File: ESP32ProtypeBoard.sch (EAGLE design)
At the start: 101 parts, among them IC1 SOIC-8, IC2 SI4431BDY, IC4 LMC555*, J10 POWER_JACKPTH_LOCK, Q1 MMBT3904*, Q2 MMBT3904, Q3 MMBT3904, U2 ESP-WROOM-32

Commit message: All connected
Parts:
- added J54: (no value), SparkFun-Connectors:CONN_10NO_SILK_PTH_FEMALE
- C2: device rcl:C-EUC1206K -> rcl:C-EUC1210
- J8: device SparkFun-Connectors:CONN_041X04_NO_SILK -> SparkFun-Connectors:CONN_111X11_NO_SILK
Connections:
- net +3V3: now also J17.4, J17.5
- net GND: now also J17.2
- net IO22: now also J17.7
- net IO23: now also J17.3
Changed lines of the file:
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@@
 <part name="R8" library="eagle-ltspice" library_urn="urn:adsk.eagle:library:217" deviceset="R" device="R1206" package3d_urn="urn:adsk.eagle:package:13301/1" value="470R"/>
 <part name="GND1" library="supply1" library_urn="urn:adsk.eagle:library:371" deviceset="GND" device=""/>
-<part name="C2" library="rcl" library_urn="urn:adsk.eagle:library:334" deviceset="C-EU" device="C1206K" package3d_urn="urn:adsk.eagle:package:23682/2" value="100uF"/>
+<part name="C2" library="rcl" library_urn="urn:adsk.eagle:library:334" deviceset="C-EU" device="C1210" package3d_urn="urn:adsk.eagle:package:23619/2" value="100uF"/>
 <part name="AMS1117-3.3" library="SparkFun-IC-Power" deviceset="V_REG_LD1117VXX" device="LD1117-SMD" value="3V3"/>
 <part name="GND11" library="supply1" library_urn="urn:adsk.eagle:library:371" deviceset="GND" device=""/>
@@
 <part name="J6" library="SparkFun-Connectors" deviceset="CONN_16" device="1X16_NO_SILK"/>
 <part name="J7" library="SparkFun-Connectors" deviceset="CONN_06X2" device="NO_SILK"/>
-<part name="J8" library="SparkFun-Connectors" deviceset="CONN_04" device="1X04_NO_SILK"/>
+<part name="J8" library="SparkFun-Connectors" library_urn="urn:adsk.eagle:library:513" deviceset="CONN_11" device="1X11_NO_SILK" package3d_urn="urn:adsk.eagle:package:38260/1"/>
 <part name="J9" library="SparkFun-Connectors" deviceset="CONN_04" device="1X04_NO_SILK"/>
 <part name="J17" library="SparkFun-Connectors" deviceset="CONN_07" device="NO_SILK"/>
@@
 <part name="GND26" library="supply1" library_urn="urn:adsk.eagle:library:371" deviceset="GND" device=""/>
 <part name="TP1" library="testpad" library_urn="urn:adsk.eagle:library:385" deviceset="TP" device="TP15SQ" package3d_urn="urn:adsk.eagle:package:27975/1" value="TPTP15SQ"/>
+<part name="J54" library="SparkFun-Connectors" library_urn="urn:adsk.eagle:library:513" deviceset="CONN_10" device="NO_SILK_PTH_FEMALE" package3d_urn="urn:adsk.eagle:package:38161/1"/>
+<part name="+3V11" library="supply1" library_urn="urn:adsk.eagle:library:371" deviceset="+3V3" device=""/>
 </parts>
 <sheets>
@@
 <attribute name="NAME" x="242.57" y="-115.57" size="1.778" layer="95" rot="R90"/>
 <attribute name="TP_SIGNAL_NAME" x="245.11" y="-113.03" size="1.778" layer="97" rot="R90"/>
+</instance>
+<instance part="J54" gate="G$1" x="154.94" y="-25.4" smashed="yes">
+<attribute name="VALUE" x="154.94" y="-48.006" size="1.778" layer="96" font="vector"/>
+<attribute name="NAME" x="154.94" y="-17.272" size="1.778" layer="95" font="vector"/>
+</instance>
+<instance part="+3V11" gate="G$1" x="198.12" y="-114.3" smashed="yes" rot="R270">
+<attribute name="VALUE" x="193.04" y="-111.76" size="1.778" layer="96"/>
 </instance>
 </instances>
@@
 <pinref part="J17" gate="G$1" pin="1"/>
 <pinref part="GND18" gate="1" pin="GND"/>
+<pinref part="J17" gate="G$1" pin="2"/>
+<wire x1="190.5" y1="-119.38" x2="190.5" y2="-121.92" width="0.1524" layer="91"/>
+<junction x="190.5" y="-121.92"/>
 </segment>
 <segment>
@@
 <wire x1="302.26" y1="78.74" x2="302.26" y2="83.82" width="0.1524" layer="91"/>
 </segment>
+<segment>
+<pinref part="J17" gate="G$1" pin="4"/>
+<wire x1="190.5" y1="-114.3" x2="195.58" y2="-114.3" width="0.1524" layer="91"/>
+<pinref part="+3V11" gate="G$1" pin="+3V3"/>
+<pinref part="J17" gate="G$1" pin="5"/>
+<wire x1="190.5" y1="-111.76" x2="190.5" y2="-114.3" width="0.1524" layer="91"/>
+<junction x="190.5" y="-114.3"/>
+</segment>
 </net>
 <net name="EN" class="0">
@@
 <junction x="236.22" y="68.58"/>
 </segment>
+<segment>
+<pinref part="J17" gate="G$1" pin="7"/>
+<wire x1="190.5" y1="-106.68" x2="195.58" y2="-106.68" width="0.1524" layer="91"/>
+<label x="190.5" y="-106.68" size="1.778" layer="95"/>
+</segment>
 </net>
 <net name="IO23" class="0">
@@
 <label x="215.9" y="76.2" size="1.778" layer="95"/>
 </segment>
-</net>
+<segment>
+<pinref part="J17" gate="G$1" pin="3"/>
+<wire x1="190.5" y1="-116.84" x2="195.58" y2="-116.84" width="0.1524" layer="91"/>
+<label x="190.5" y="-116.84" size="1.778" layer="95"/>
+</segment>
+</net>

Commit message: Moving around some pins
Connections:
- net IO0: now also IO2.2
- net IO15: now also J16.1; no longer J12.11, J31.11
- net IO2: now also J12.11, J31.11; no longer IO2.2
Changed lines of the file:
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@@
 <wire x1="368.3" y1="73.66" x2="368.3" y2="71.12" width="0.1524" layer="91"/>
+</segment>
+<segment>
+<pinref part="IO2" gate="G$1" pin="2"/>
+<wire x1="210.82" y1="17.78" x2="215.9" y2="17.78" width="0.1524" layer="91"/>
+<label x="210.82" y="17.78" size="1.778" layer="95"/>
 </segment>
 </net>
@@
 </segment>
 <segment>
-<pinref part="J12" gate="G$1" pin="11"/>
-<wire x1="236.22" y1="45.72" x2="228.6" y2="45.72" width="0.1524" layer="91"/>
-<label x="228.6" y="45.72" size="1.778" layer="95"/>
-<pinref part="J31" gate="G$1" pin="11"/>
-<wire x1="236.22" y1="45.72" x2="243.84" y2="45.72" width="0.1524" layer="91"/>
-<junction x="236.22" y="45.72"/>
+<pinref part="J16" gate="G$1" pin="1"/>
+<wire x1="68.58" y1="-68.58" x2="73.66" y2="-68.58" width="0.1524" layer="91"/>
+<label x="68.58" y="-68.58" size="1.778" layer="95"/>
 </segment>
 </net>
@@
 </segment>
 <segment>
-<pinref part="IO2" gate="G$1" pin="2"/>
-<wire x1="210.82" y1="17.78" x2="215.9" y2="17.78" width="0.1524" layer="91"/>
-<label x="210.82" y="17.78" size="1.778" layer="95"/>
-</segment>
-</net>
+<pinref part="J12" gate="G$1" pin="11"/>
+<wire x1="236.22" y1="45.72" x2="228.6" y2="45.72" width="0.1524" layer="91"/>
+<label x="228.6" y="45.72" size="1.778" layer="95"/>
+<pinref part="J31" gate="G$1" pin="11"/>
+<wire x1="236.22" y1="45.72" x2="243.84" y2="45.72" width="0.1524" layer="91"/>
+<junction x="236.22" y="45.72"/>
+</segment>
+</net>

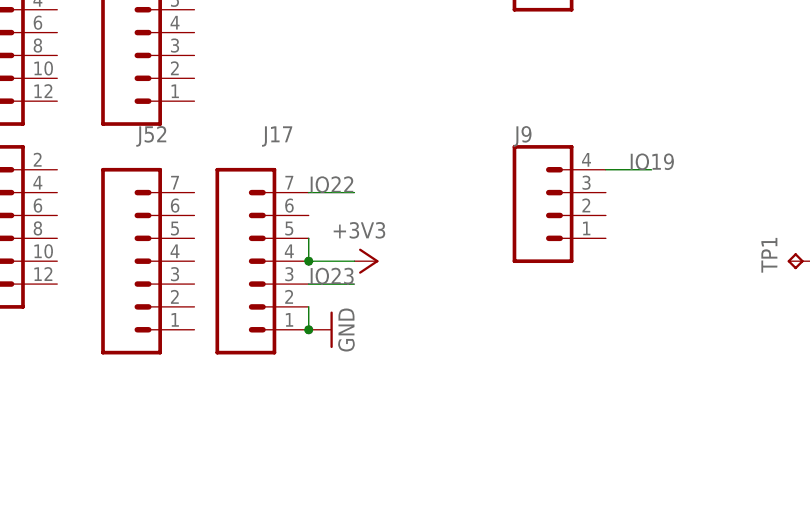
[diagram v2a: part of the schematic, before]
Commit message: More silk tuning
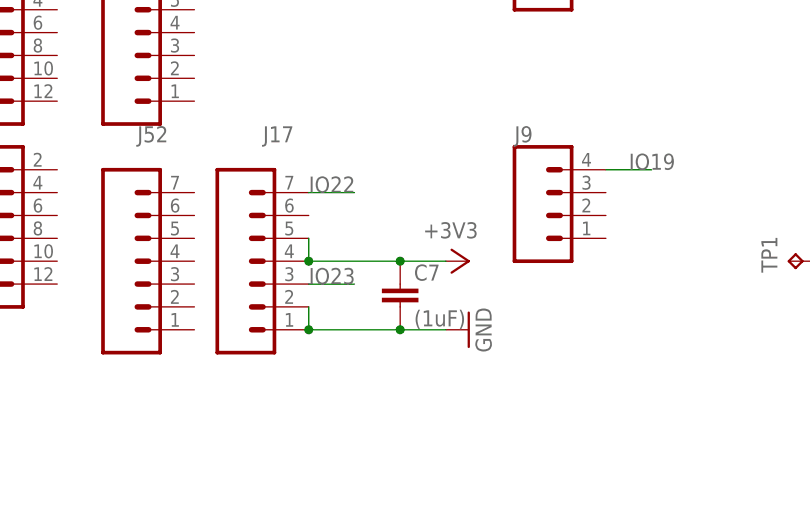
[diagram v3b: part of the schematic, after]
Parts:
- added C7: (1uF), rcl:C-EUC1206
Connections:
- net +3V3: now also C7.1
- net GND: now also C7.2
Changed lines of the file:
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@@
 <part name="J54" library="SparkFun-Connectors" library_urn="urn:adsk.eagle:library:513" deviceset="CONN_10" device="NO_SILK_PTH_FEMALE" package3d_urn="urn:adsk.eagle:package:38161/1"/>
 <part name="+3V11" library="supply1" library_urn="urn:adsk.eagle:library:371" deviceset="+3V3" device=""/>
+<part name="C7" library="rcl" library_urn="urn:adsk.eagle:library:334" deviceset="C-EU" device="C1206" package3d_urn="urn:adsk.eagle:package:23618/2" value="(1uF)"/>
 </parts>
 <sheets>
@@
 <attribute name="VALUE" x="351.79" y="75.438" size="1.778" layer="96"/>
 </instance>
-<instance part="GND18" gate="1" x="193.04" y="-121.92" smashed="yes" rot="R90">
-<attribute name="VALUE" x="195.58" y="-124.46" size="1.778" layer="96" rot="R90"/>
+<instance part="GND18" gate="1" x="208.28" y="-121.92" smashed="yes" rot="R90">
+<attribute name="VALUE" x="210.82" y="-124.46" size="1.778" layer="96" rot="R90"/>
 </instance>
 <instance part="GND26" gate="1" x="251.46" y="-114.3" smashed="yes" rot="R90">
@@
 <attribute name="NAME" x="154.94" y="-17.272" size="1.778" layer="95" font="vector"/>
 </instance>
-<instance part="+3V11" gate="G$1" x="198.12" y="-114.3" smashed="yes" rot="R270">
-<attribute name="VALUE" x="193.04" y="-111.76" size="1.778" layer="96"/>
+<instance part="+3V11" gate="G$1" x="208.28" y="-114.3" smashed="yes" rot="R270">
+<attribute name="VALUE" x="203.2" y="-111.76" size="1.778" layer="96"/>
+</instance>
+<instance part="C7" gate="G$1" x="200.66" y="-116.84" smashed="yes">
+<attribute name="NAME" x="202.184" y="-116.459" size="1.778" layer="95"/>
+<attribute name="VALUE" x="202.184" y="-121.539" size="1.778" layer="96"/>
 </instance>
 </instances>
@@
 <pinref part="GND18" gate="1" pin="GND"/>
 <pinref part="J17" gate="G$1" pin="2"/>
+<wire x1="205.74" y1="-121.92" x2="200.66" y2="-121.92" width="0.1524" layer="91"/>
+<pinref part="C7" gate="G$1" pin="2"/>
+<wire x1="200.66" y1="-121.92" x2="190.5" y2="-121.92" width="0.1524" layer="91"/>
+<junction x="200.66" y="-121.92"/>
 <wire x1="190.5" y1="-119.38" x2="190.5" y2="-121.92" width="0.1524" layer="91"/>
 <junction x="190.5" y="-121.92"/>
@@
 <segment>
 <pinref part="J17" gate="G$1" pin="4"/>
-<wire x1="190.5" y1="-114.3" x2="195.58" y2="-114.3" width="0.1524" layer="91"/>
+<wire x1="190.5" y1="-114.3" x2="200.66" y2="-114.3" width="0.1524" layer="91"/>
 <pinref part="+3V11" gate="G$1" pin="+3V3"/>
 <pinref part="J17" gate="G$1" pin="5"/>
+<wire x1="200.66" y1="-114.3" x2="205.74" y2="-114.3" width="0.1524" layer="91"/>
 <wire x1="190.5" y1="-111.76" x2="190.5" y2="-114.3" width="0.1524" layer="91"/>
 <junction x="190.5" y="-114.3"/>
+<pinref part="C7" gate="G$1" pin="1"/>
+<junction x="200.66" y="-114.3"/>
 </segment>
 </net>

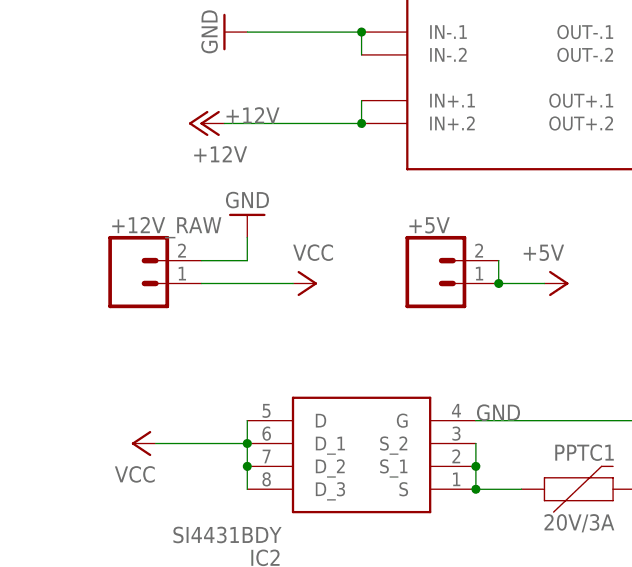
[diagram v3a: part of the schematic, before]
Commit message: Replaced VCC IN pins to accomodate large screw terminal
Some more silk changes
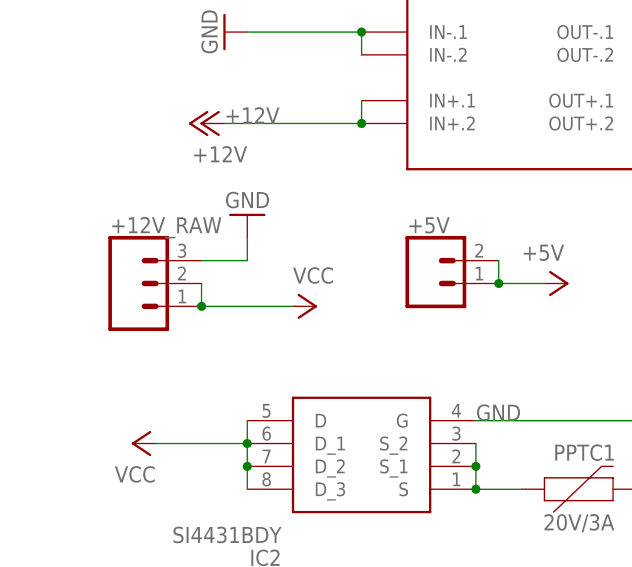
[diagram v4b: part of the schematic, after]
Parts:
- +12V_RAW: device SparkFun-Connectors:CONN_02PTH3 -> SparkFun-Connectors:CONN_03LONGPADS
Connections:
- net GND: now also +12V_RAW.3; no longer +12V_RAW.2
- net VCC: now also +12V_RAW.2
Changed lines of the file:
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@@
 <grid distance="0.1" unitdist="inch" unit="inch" style="lines" multiple="1" display="no" altdistance="0.01" altunitdist="inch" altunit="inch"/>
 <layers>
-<layer number="1" name="Top" color="4" fill="1" visible="yes" active="no"/>
-<layer number="16" name="Bottom" color="1" fill="1" visible="yes" active="no"/>
-<layer number="17" name="Pads" color="2" fill="1" visible="yes" active="no"/>
-<layer number="18" name="Vias" color="2" fill="1" visible="yes" active="no"/>
-<layer number="19" name="Unrouted" color="6" fill="1" visible="yes" active="no"/>
-<layer number="20" name="Dimension" color="24" fill="1" visible="yes" active="no"/>
-<layer number="21" name="tPlace" color="7" fill="1" visible="yes" active="no"/>
-<layer number="22" name="bPlace" color="7" fill="1" visible="yes" active="no"/>
-<layer number="23" name="tOrigins" color="15" fill="1" visible="yes" active="no"/>
-<layer number="24" name="bOrigins" color="15" fill="1" visible="yes" active="no"/>
-<layer number="25" name="tNames" color="7" fill="1" visible="yes" active="no"/>
-<layer number="26" name="bNames" color="7" fill="1" visible="yes" active="no"/>
-<layer number="27" name="tValues" color="7" fill="1" visible="yes" active="no"/>
-<layer number="28" name="bValues" color="7" fill="1" visible="yes" active="no"/>
+<layer number="1" name="Top" color="4" fill="1" visible="no" active="no"/>
+<layer number="16" name="Bottom" color="1" fill="1" visible="no" active="no"/>
+<layer number="17" name="Pads" color="2" fill="1" visible="no" active="no"/>
+<layer number="18" name="Vias" color="2" fill="1" visible="no" active="no"/>
+<layer number="19" name="Unrouted" color="6" fill="1" visible="no" active="no"/>
+<layer number="20" name="Dimension" color="24" fill="1" visible="no" active="no"/>
+<layer number="21" name="tPlace" color="7" fill="1" visible="no" active="no"/>
+<layer number="22" name="bPlace" color="7" fill="1" visible="no" active="no"/>
+<layer number="23" name="tOrigins" color="15" fill="1" visible="no" active="no"/>
+<layer number="24" name="bOrigins" color="15" fill="1" visible="no" active="no"/>
+<layer number="25" name="tNames" color="7" fill="1" visible="no" active="no"/>
+<layer number="26" name="bNames" color="7" fill="1" visible="no" active="no"/>
+<layer number="27" name="tValues" color="7" fill="1" visible="no" active="no"/>
+<layer number="28" name="bValues" color="7" fill="1" visible="no" active="no"/>
 <layer number="29" name="tStop" color="7" fill="3" visible="no" active="no"/>
 <layer number="30" name="bStop" color="7" fill="6" visible="no" active="no"/>
@@
 <layer number="35" name="tGlue" color="7" fill="4" visible="no" active="no"/>
 <layer number="36" name="bGlue" color="7" fill="5" visible="no" active="no"/>
-<layer number="37" name="tTest" color="7" fill="1" visible="yes" active="no"/>
-<layer number="38" name="bTest" color="7" fill="1" visible="yes" active="no"/>
+<layer number="37" name="tTest" color="7" fill="1" visible="no" active="no"/>
+<layer number="38" name="bTest" color="7" fill="1" visible="no" active="no"/>
 <layer number="39" name="tKeepout" color="4" fill="11" visible="no" active="no"/>
 <layer number="40" name="bKeepout" color="1" fill="11" visible="no" active="no"/>
@@
 <layer number="44" name="Drills" color="7" fill="1" visible="no" active="no"/>
 <layer number="45" name="Holes" color="7" fill="1" visible="no" active="no"/>
-<layer number="46" name="Milling" color="3" fill="1" visible="yes" active="no"/>
-<layer number="47" name="Measures" color="7" fill="1" visible="yes" active="no"/>
-<layer number="48" name="Document" color="7" fill="1" visible="yes" active="no"/>
-<layer number="49" name="Reference" color="7" fill="1" visible="yes" active="no"/>
-<layer number="50" name="dxf" color="7" fill="1" visible="yes" active="no"/>
-<layer number="51" name="tDocu" color="7" fill="1" visible="yes" active="no"/>
-<layer number="52" name="bDocu" color="7" fill="1" visible="yes" active="no"/>
-<layer number="53" name="tGND_GNDA" color="7" fill="9" visible="yes" active="no"/>
-<layer number="54" name="bGND_GNDA" color="1" fill="9" visible="yes" active="no"/>
-<layer number="56" name="wert" color="7" fill="1" visible="yes" active="no"/>
-<layer number="57" name="tCAD" color="7" fill="1" visible="yes" active="no"/>
-<layer number="59" name="tCarbon" color="7" fill="1" visible="yes" active="no"/>
-<layer number="60" name="bCarbon" color="7" fill="1" visible="yes" active="no"/>
+<layer number="46" name="Milling" color="3" fill="1" visible="no" active="no"/>
+<layer number="47" name="Measures" color="7" fill="1" visible="no" active="no"/>
+<layer number="48" name="Document" color="7" fill="1" visible="no" active="no"/>
+<layer number="49" name="Reference" color="7" fill="1" visible="no" active="no"/>
+<layer number="50" name="dxf" color="7" fill="1" visible="no" active="no"/>
+<layer number="51" name="tDocu" color="7" fill="1" visible="no" active="no"/>
+<layer number="52" name="bDocu" color="7" fill="1" visible="no" active="no"/>
+<layer number="53" name="tGND_GNDA" color="7" fill="9" visible="no" active="no"/>
+<layer number="54" name="bGND_GNDA" color="1" fill="9" visible="no" active="no"/>
+<layer number="56" name="wert" color="7" fill="1" visible="no" active="no"/>
+<layer number="57" name="tCAD" color="7" fill="1" visible="no" active="no"/>
+<layer number="59" name="tCarbon" color="7" fill="1" visible="no" active="no"/>
+<layer number="60" name="bCarbon" color="7" fill="1" visible="no" active="no"/>
 <layer number="88" name="SimResults" color="9" fill="1" visible="yes" active="yes"/>
 <layer number="89" name="SimProbes" color="9" fill="1" visible="yes" active="yes"/>
@@
 <part name="GND13" library="supply1" library_urn="urn:adsk.eagle:library:371" deviceset="GND" device=""/>
 <part name="+5V" library="SparkFun-Connectors" deviceset="CONN_02" device="1X02_NO_SILK"/>
-<part name="+12V_RAW" library="SparkFun-Connectors" deviceset="CONN_02" device="PTH3"/>
+<part name="+12V_RAW" library="SparkFun-Connectors" library_urn="urn:adsk.eagle:library:513" deviceset="CONN_03" device="LONGPADS" package3d_urn="urn:adsk.eagle:package:38068/1"/>
 <part name="GND" library="SparkFun-Connectors" deviceset="CONN_02" device="1X02_NO_SILK"/>
 <part name="GND14" library="supply1" library_urn="urn:adsk.eagle:library:371" deviceset="GND" device=""/>
@@
 <attribute name="NAME" x="50.8" y="41.148" size="1.778" layer="95" font="vector"/>
 </instance>
-<instance part="+12V_RAW" gate="G$1" x="20.32" y="35.56" smashed="yes">
+<instance part="+12V_RAW" gate="J$1" x="20.32" y="35.56" smashed="yes">
 <attribute name="VALUE" x="17.78" y="30.734" size="1.778" layer="96" font="vector"/>
 <attribute name="NAME" x="17.78" y="41.148" size="1.778" layer="95" font="vector"/>
@@
 <attribute name="VALUE" x="116.84" y="2.54" size="1.778" layer="96"/>
 </instance>
-<instance part="P+10" gate="VCC" x="40.64" y="35.56" smashed="yes" rot="R270">
-<attribute name="VALUE" x="38.1" y="38.1" size="1.778" layer="96"/>
+<instance part="P+10" gate="VCC" x="40.64" y="33.02" smashed="yes" rot="R270">
+<attribute name="VALUE" x="38.1" y="35.56" size="1.778" layer="96"/>
 </instance>
 <instance part="+3V6" gate="G$1" x="165.1" y="43.18" smashed="yes" rot="R270">
@@
 </segment>
 <segment>
-<pinref part="+12V_RAW" gate="G$1" pin="2"/>
-<wire x1="27.94" y1="38.1" x2="33.02" y2="38.1" width="0.1524" layer="91"/>
 <pinref part="GND7" gate="1" pin="GND"/>
 <wire x1="33.02" y1="38.1" x2="33.02" y2="40.64" width="0.1524" layer="91"/>
+<pinref part="+12V_RAW" gate="J$1" pin="3"/>
+<wire x1="27.94" y1="38.1" x2="33.02" y2="38.1" width="0.1524" layer="91"/>
 </segment>
 <segment>
@@
 </segment>
 <segment>
-<pinref part="+12V_RAW" gate="G$1" pin="1"/>
-<wire x1="38.1" y1="35.56" x2="27.94" y2="35.56" width="0.1524" layer="91"/>
+<pinref part="+12V_RAW" gate="J$1" pin="1"/>
+<wire x1="38.1" y1="33.02" x2="27.94" y2="33.02" width="0.1524" layer="91"/>
 <pinref part="P+10" gate="VCC" pin="VCC"/>
-</segment>
-<segment>
+<pinref part="+12V_RAW" gate="J$1" pin="2"/>
+<wire x1="27.94" y1="35.56" x2="27.94" y2="33.02" width="0.1524" layer="91"/>
+<junction x="27.94" y="33.02"/>
+</segment>
+<segment>
